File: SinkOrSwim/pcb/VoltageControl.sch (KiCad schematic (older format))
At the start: 7 parts

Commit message: First annotation
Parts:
- gave numbers to parts that had none: 7
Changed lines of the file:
@@
 $EndDescr
 $Comp
-L R R?
+L R R301
 U 1 1 54DC6887
 P 4450 4900
-F 0 "R?" V 4530 4900 50  0000 C CNN
+F 0 "R301" V 4530 4900 50  0000 C CNN
 F 1 "R" V 4457 4901 50  0000 C CNN
 F 2 "" V 4380 4900 30  0000 C CNN
@@
 $EndComp
 $Comp
-L GND #PWR?
+L GND #PWR302
 U 1 1 54DC688E
 P 6000 3950
-F 0 "#PWR?" H 6000 3700 60  0001 C CNN
+F 0 "#PWR302" H 6000 3700 60  0001 C CNN
 F 1 "GND" H 6000 3800 60  0000 C CNN
 F 2 "" H 6000 3950 60  0000 C CNN
@@
 	4450 5600 9350 5600
 $Comp
-L POT RV?
+L POT RV301
 U 1 1 54DC689F
 P 4450 4050
-F 0 "RV?" H 4450 3950 50  0000 C CNN
+F 0 "RV301" H 4450 3950 50  0000 C CNN
 F 1 "POT" H 4450 4050 50  0000 C CNN
 F 2 "" H 4450 4050 60  0000 C CNN
@@
 2.7V
 $Comp
-L C C?
+L C C301
 U 1 1 54DC68AA
 P 5350 2750
-F 0 "C?" H 5400 2850 50  0000 L CNN
+F 0 "C301" H 5400 2850 50  0000 L CNN
 F 1 "C" H 5400 2650 50  0000 L CNN
 F 2 "" H 5388 2600 30  0000 C CNN
@@
 Connection ~ 5350 2400
 $Comp
-L GND #PWR?
+L GND #PWR301
 U 1 1 54DC68B3
 P 5350 3000
-F 0 "#PWR?" H 5350 2750 60  0001 C CNN
+F 0 "#PWR301" H 5350 2750 60  0001 C CNN
 F 1 "GND" H 5350 2850 60  0000 C CNN
 F 2 "" H 5350 3000 60  0000 C CNN
@@
 	5350 3000 5350 2950
 $Comp
-L LMV358 U?
+L LMV358 U201
 U 2 1 54DC68BA
 P 6100 3350
-F 0 "U?" H 6050 3550 60  0000 L CNN
+F 0 "U201" H 6050 3550 60  0000 L CNN
 F 1 "LMV358" H 6050 3100 60  0000 L CNN
 F 2 "" H 6100 3350 60  0000 C CNN
@@
 	4600 1900 4600 4050
 $Comp
-L DIODE D?
+L DIODE D301
 U 1 1 54DC6A11
 P 7000 3350
-F 0 "D?" H 7000 3450 50  0000 C CNN
+F 0 "D301" H 7000 3450 50  0000 C CNN
 F 1 "DIODE" H 7000 3250 50  0000 C CNN
 F 2 "" H 7000 3350 60  0000 C CNN
@@
 	6800 3350 6600 3350
 $Comp
-L R R?
+L R R302
 U 1 1 54DC6B1A
 P 8500 3900
-F 0 "R?" V 8580 3900 50  0000 C CNN
+F 0 "R302" V 8580 3900 50  0000 C CNN
 F 1 "9K" V 8507 3901 50  0000 C CNN
 F 2 "" V 8430 3900 30  0000 C CNN
@@
 $EndComp
 $Comp
-L R R?
+L R R303
 U 1 1 54DC6B7F
 P 8500 4750
-F 0 "R?" V 8580 4750 50  0000 C CNN
+F 0 "R303" V 8580 4750 50  0000 C CNN
 F 1 "1K" V 8507 4751 50  0000 C CNN
 F 2 "" V 8430 4750 30  0000 C CNN

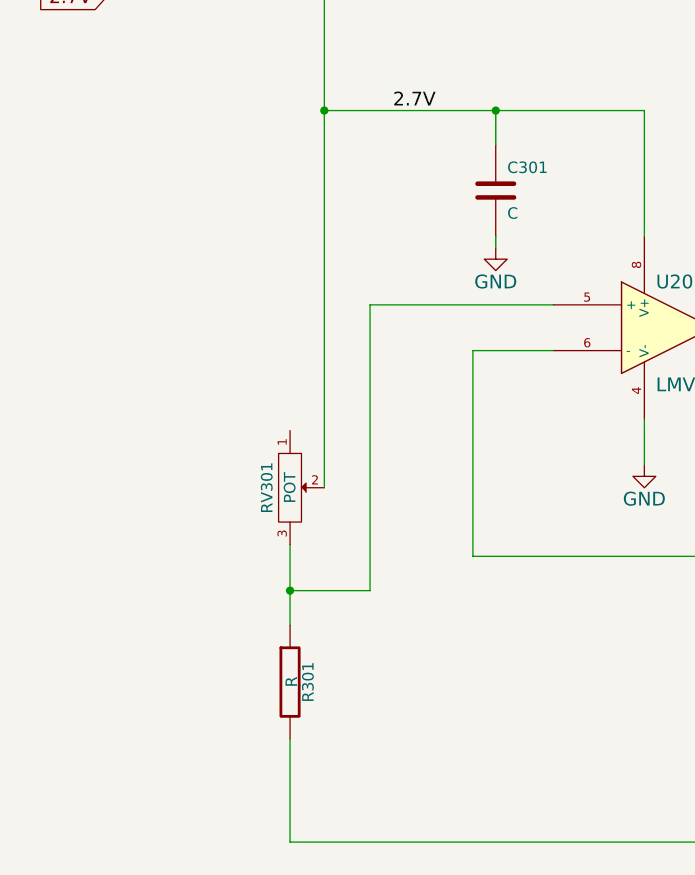
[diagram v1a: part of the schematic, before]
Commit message: Footprints associated and parts on pcb
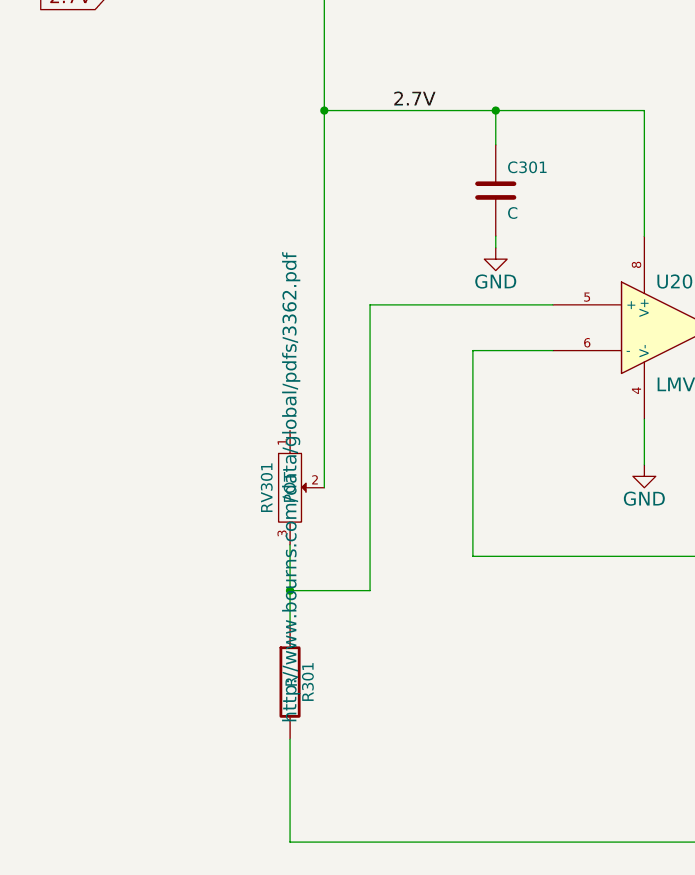
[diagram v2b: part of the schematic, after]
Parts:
- C301: footprint (none) -> Capacitors_SMD:C_0805_HandSoldering
- D301: footprint (none) -> Diodes_SMD:Diode-SMA_Handsoldering; MPN (none) -> RS1M-13-F
- R301, R302, R303: footprint (none) -> Resistors_SMD:R_0805_HandSoldering
- RV301: footprint (none) -> pcb:Potiometer_Bourns_3362P; MPN (none) -> 3362P-1
- U201: footprint (none) -> SMD_Packages:SOIC-8-N; MPN (none) -> LMV358IDT
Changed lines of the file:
@@
 F 0 "R301" V 4530 4900 50  0000 C CNN
 F 1 "R" V 4457 4901 50  0000 C CNN
-F 2 "" V 4380 4900 30  0000 C CNN
+F 2 "Resistors_SMD:R_0805_HandSoldering" V 4380 4900 30  0001 C CNN
 F 3 "" H 4450 4900 30  0000 C CNN
 	1    4450 4900
@@
 $EndComp
 $Comp
-L GND #PWR302
+L GND #PWR05
 U 1 1 54DC688E
 P 6000 3950
-F 0 "#PWR302" H 6000 3700 60  0001 C CNN
+F 0 "#PWR05" H 6000 3700 60  0001 C CNN
 F 1 "GND" H 6000 3800 60  0000 C CNN
 F 2 "" H 6000 3950 60  0000 C CNN
@@
 F 0 "RV301" H 4450 3950 50  0000 C CNN
 F 1 "POT" H 4450 4050 50  0000 C CNN
-F 2 "" H 4450 4050 60  0000 C CNN
-F 3 "" H 4450 4050 60  0000 C CNN
+F 2 "pcb:Potiometer_Bourns_3362P" H 4450 4050 60  0001 C CNN
+F 3 "http://www.bourns.com/data/global/pdfs/3362.pdf" H 4450 4050 60  0000 C CNN
+F 4 "3362P-1" H 4450 4050 60  0001 C CNN "MPN"
 	1    4450 4050
 	0    1    1    0
@@
 F 0 "C301" H 5400 2850 50  0000 L CNN
 F 1 "C" H 5400 2650 50  0000 L CNN
-F 2 "" H 5388 2600 30  0000 C CNN
+F 2 "Capacitors_SMD:C_0805_HandSoldering" H 5388 2600 30  0001 C CNN
 F 3 "" H 5350 2750 60  0000 C CNN
 	1    5350 2750
@@
 Connection ~ 5350 2400
 $Comp
-L GND #PWR301
+L GND #PWR06
 U 1 1 54DC68B3
 P 5350 3000
-F 0 "#PWR301" H 5350 2750 60  0001 C CNN
+F 0 "#PWR06" H 5350 2750 60  0001 C CNN
 F 1 "GND" H 5350 2850 60  0000 C CNN
 F 2 "" H 5350 3000 60  0000 C CNN
@@
 F 0 "U201" H 6050 3550 60  0000 L CNN
 F 1 "LMV358" H 6050 3100 60  0000 L CNN
-F 2 "" H 6100 3350 60  0000 C CNN
-F 3 "" H 6100 3350 60  0000 C CNN
+F 2 "SMD_Packages:SOIC-8-N" H 6100 3350 60  0001 C CNN
+F 3 "http://www.st.com/web/en/resource/technical/document/datasheet/CD00079372.pdf" H 6100 3350 60  0001 C CNN
+F 4 "LMV358IDT" H 6100 3350 60  0001 C CNN "MPN"
 	2    6100 3350
 	1    0    0    -1
@@
 F 0 "D301" H 7000 3450 50  0000 C CNN
 F 1 "DIODE" H 7000 3250 50  0000 C CNN
-F 2 "" H 7000 3350 60  0000 C CNN
-F 3 "" H 7000 3350 60  0000 C CNN
+F 2 "Diodes_SMD:Diode-SMA_Handsoldering" H 7000 3350 60  0001 C CNN
+F 3 "http://www.diodes.com/datasheets/ds15002.pdf" H 7000 3350 60  0001 C CNN
+F 4 "RS1M-13-F" H 7000 3350 60  0001 C CNN "MPN"
 	1    7000 3350
 	-1   0    0    1
@@
 F 0 "R302" V 8580 3900 50  0000 C CNN
 F 1 "9K" V 8507 3901 50  0000 C CNN
-F 2 "" V 8430 3900 30  0000 C CNN
+F 2 "Resistors_SMD:R_0805_HandSoldering" V 8430 3900 30  0001 C CNN
 F 3 "" H 8500 3900 30  0000 C CNN
 	1    8500 3900
@@
 F 0 "R303" V 8580 4750 50  0000 C CNN
 F 1 "1K" V 8507 4751 50  0000 C CNN
-F 2 "" V 8430 4750 30  0000 C CNN
+F 2 "Resistors_SMD:R_0805_HandSoldering" V 8430 4750 30  0001 C CNN
 F 3 "" H 8500 4750 30  0000 C CNN
 	1    8500 4750

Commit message: Fixed some drc items and started on heatsink footprint.
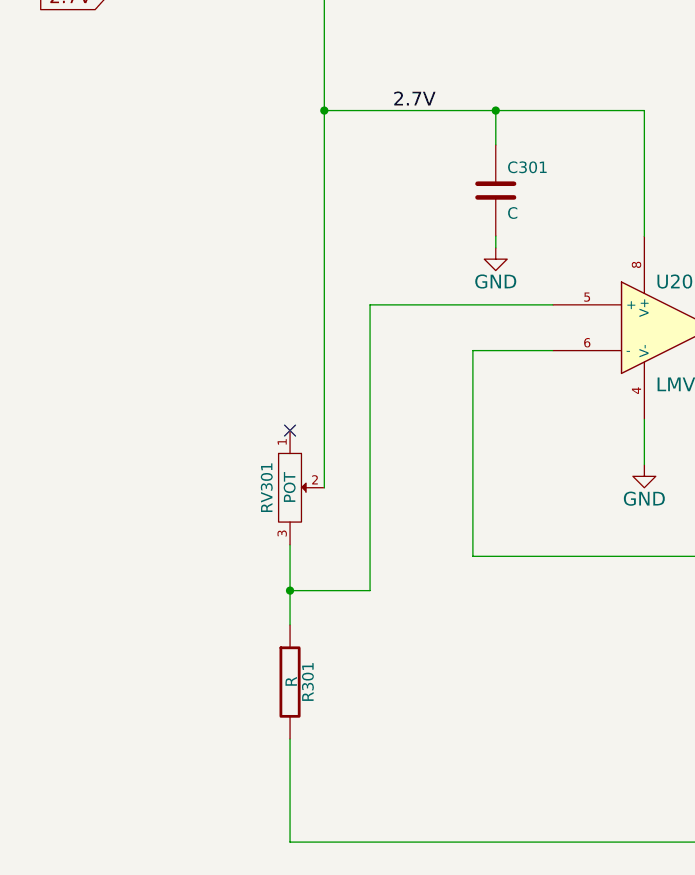
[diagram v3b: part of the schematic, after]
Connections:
- no-connect marks 0 -> 1
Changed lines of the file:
@@
 F 1 "POT" H 4450 4050 50  0000 C CNN
 F 2 "pcb:Potiometer_Bourns_3362P" H 4450 4050 60  0001 C CNN
-F 3 "http://www.bourns.com/data/global/pdfs/3362.pdf" H 4450 4050 60  0000 C CNN
+F 3 "http://www.bourns.com/data/global/pdfs/3362.pdf" H 4450 4050 60  0001 C CNN
 F 4 "3362P-1" H 4450 4050 60  0001 C CNN "MPN"
 	1    4450 4050
@@
 Text HLabel 9350 5600 2    60   Input ~ 0
 Curent_Sink-
+NoConn ~ 4450 3800
 $EndSCHEMATC

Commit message: Find new terminal blocks.  Set resistor divider values.  Rearrange POT and fixed resistor.
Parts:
- R301: value R -> 28.7K; MPN (none) -> Value
- RV301: value POT -> 10K
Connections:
- net 2.7V: now also R301.1; no longer RV301.2
- net Curent_Sink-: now also RV301.3; no longer R301.2
- new net: R301.2, RV301.2, U201.5 (+)
- no-connect marks 1 -> 0
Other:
- note added: "0-20V"
- note added: "0-2V"
- moved on the sheet: R301, RV301
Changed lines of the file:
@@
 L R R301
 U 1 1 54DC6887
-P 4450 4900
-F 0 "R301" V 4530 4900 50  0000 C CNN
-F 1 "R" V 4457 4901 50  0000 C CNN
-F 2 "Resistors_SMD:R_0805_HandSoldering" V 4380 4900 30  0001 C CNN
-F 3 "" H 4450 4900 30  0000 C CNN
-	1    4450 4900
+P 4600 4150
+F 0 "R301" V 4680 4150 50  0000 C CNN
+F 1 "28.7K" V 4607 4151 50  0000 C CNN
+F 2 "Resistors_SMD:R_0805_HandSoldering" V 4530 4150 30  0001 C CNN
+F 3 "" H 4600 4150 30  0000 C CNN
+F 4 "Value" H 4600 4150 60  0001 C CNN "MPN"
+	1    4600 4150
 	1    0    0    -1
 $EndComp
@@
 	5250 4350 8500 4350
 Wire Wire Line
-	4450 4300 4450 4650
-Wire Wire Line
-	4450 4500 4800 4500
-Wire Wire Line
-	4800 4500 4800 3250
+	4800 4750 4800 3250
 Wire Wire Line
 	4800 3250 5600 3250
-Connection ~ 4450 4500
 Wire Wire Line
-	4450 5150 4450 5600
+	4200 5000 4200 5600
 Wire Wire Line
-	4450 5600 9350 5600
+	4200 5600 9350 5600
 $Comp
 L POT RV301
 U 1 1 54DC689F
-P 4450 4050
-F 0 "RV301" H 4450 3950 50  0000 C CNN
-F 1 "POT" H 4450 4050 50  0000 C CNN
-F 2 "pcb:Potiometer_Bourns_3362P" H 4450 4050 60  0001 C CNN
-F 3 "http://www.bourns.com/data/global/pdfs/3362.pdf" H 4450 4050 60  0001 C CNN
-F 4 "3362P-1" H 4450 4050 60  0001 C CNN "MPN"
-	1    4450 4050
+P 4200 4750
+F 0 "RV301" H 4200 4650 50  0000 C CNN
+F 1 "10K" H 4200 4750 50  0000 C CNN
+F 2 "pcb:Potiometer_Bourns_3362P" H 4200 4750 60  0001 C CNN
+F 3 "http://www.bourns.com/data/global/pdfs/3362.pdf" H 4200 4750 60  0001 C CNN
+F 4 "3362P-1" H 4200 4750 60  0001 C CNN "MPN"
+	1    4200 4750
 	0    1    1    0
 $EndComp
@@
 Wire Wire Line
 	3650 1900 4600 1900
-Wire Wire Line
-	4600 1900 4600 4050
 $Comp
 L DIODE D301
@@
 Text HLabel 9350 5600 2    60   Input ~ 0
 Curent_Sink-
-NoConn ~ 4450 3800
+Wire Wire Line
+	4350 4750 4800 4750
+Wire Wire Line
+	4600 1900 4600 3900
+Wire Wire Line
+	4600 4400 4600 4750
+Connection ~ 4600 4750
+Text Notes 5100 3350 0    60   ~ 0
+0-2V
+Text Notes 7200 4450 0    60   ~ 0
+0-2V
+Text Notes 8850 3650 0    60   ~ 0
+0-20V
 $EndSCHEMATC

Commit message: Hide some of the labels on the pcb.  Moved the ground plane to the bottom.  More work reconnecting to do.
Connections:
- no-connect marks 0 -> 1
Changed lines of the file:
@@
 Text Notes 8850 3650 0    60   ~ 0
 0-20V
+NoConn ~ 4200 4500
 $EndSCHEMATC

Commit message: Gerbers added, BOM written
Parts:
- C301: value C -> .1uf; MPN (none) -> 08055C104JAT2A
- R301: MPN Value -> RMCF0805FT28K7
- R302: MPN (none) -> RMCF0805FT9K10
- R303: MPN (none) -> RMCF0805FT1K00
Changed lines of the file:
@@
 F 1 "28.7K" V 4607 4151 50  0000 C CNN
 F 2 "Resistors_SMD:R_0805_HandSoldering" V 4530 4150 30  0001 C CNN
-F 3 "" H 4600 4150 30  0000 C CNN
-F 4 "Value" H 4600 4150 60  0001 C CNN "MPN"
+F 3 "http://www.seielect.com/Catalog/SEI-RMCF_RMCP.pdf" H 4600 4150 30  0001 C CNN
+F 4 "RMCF0805FT28K7" H 4600 4150 60  0001 C CNN "MPN"
 	1    4600 4150
 	1    0    0    -1
@@
 P 5350 2750
 F 0 "C301" H 5400 2850 50  0000 L CNN
-F 1 "C" H 5400 2650 50  0000 L CNN
+F 1 ".1uf" H 5400 2650 50  0000 L CNN
 F 2 "Capacitors_SMD:C_0805_HandSoldering" H 5388 2600 30  0001 C CNN
-F 3 "" H 5350 2750 60  0000 C CNN
+F 3 "http://www.avx.com/docs/Catalogs/cx7r.pdf" H 5350 2750 60  0001 C CNN
+F 4 "08055C104JAT2A" H 5350 2750 60  0001 C CNN "MPN"
 	1    5350 2750
 	1    0    0    -1
@@
 F 1 "9K" V 8507 3901 50  0000 C CNN
 F 2 "Resistors_SMD:R_0805_HandSoldering" V 8430 3900 30  0001 C CNN
-F 3 "" H 8500 3900 30  0000 C CNN
+F 3 "http://www.seielect.com/Catalog/SEI-RMCF_RMCP.pdf" H 8500 3900 30  0001 C CNN
+F 4 "RMCF0805FT9K10" H 8500 3900 60  0001 C CNN "MPN"
 	1    8500 3900
 	1    0    0    -1
@@
 F 1 "1K" V 8507 4751 50  0000 C CNN
 F 2 "Resistors_SMD:R_0805_HandSoldering" V 8430 4750 30  0001 C CNN
-F 3 "" H 8500 4750 30  0000 C CNN
+F 3 "http://www.seielect.com/Catalog/SEI-RMCF_RMCP.pdf" H 8500 4750 30  0001 C CNN
+F 4 "RMCF0805FT1K00" H 8500 4750 60  0001 C CNN "MPN"
 	1    8500 4750
 	1    0    0    -1
